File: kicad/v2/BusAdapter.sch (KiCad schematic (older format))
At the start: 53 parts, among them J1 Conn_02x17_Odd_Even, J10 Conn_02x06_Odd_Even, J11 Conn_02x02_Odd_Even, J12 Conn_02x06_Top_Bottom, J2 Conn_02x20_Odd_Even, J3 Conn_02x20_Odd_Even, J4 Conn_02x06_Top_Bottom, J5 Conn_02x06_Top_Bottom, J6 Conn_Coaxial, J7 Conn_Coaxial, J8 Conn_01x02_Male, J9 Conn_01x02_Male, Q1 2N3904, Q2 2N3904, SW1 SW_Push, SW2 SW_Push, U1 74LVC245, U2 74LVC245, U3 74LVC245, U4 IS61C5128AL-10TLI, U5 MCP4822

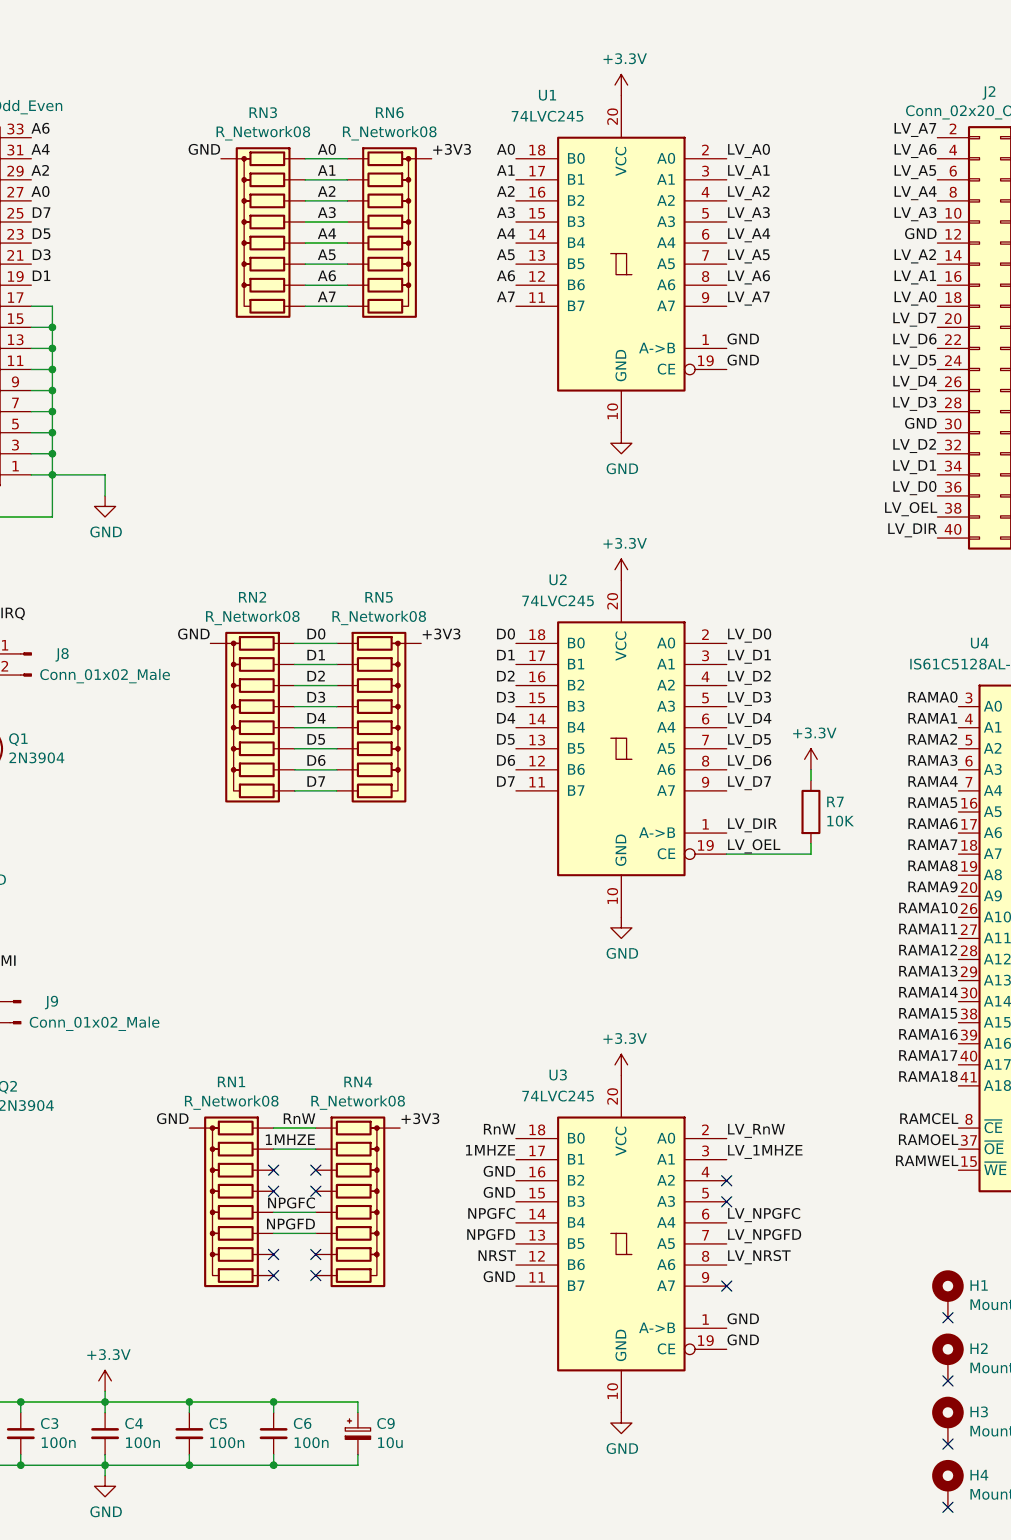
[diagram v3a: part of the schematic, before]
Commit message: PCB v2: Enlarged IDC connector holes; added power connector
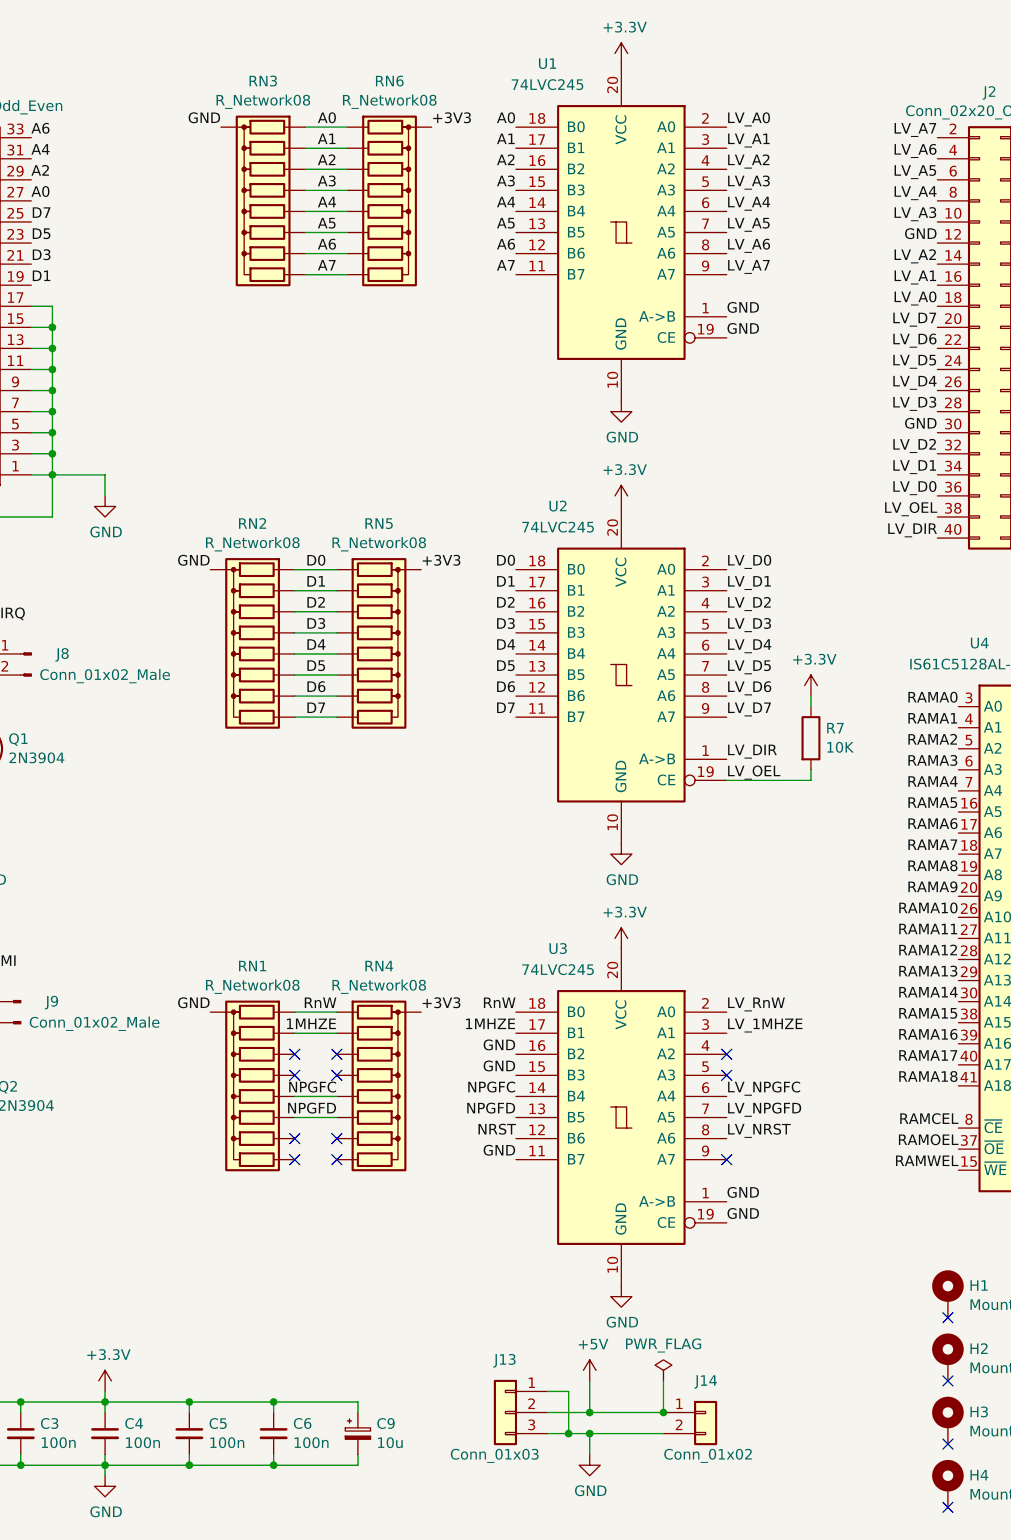
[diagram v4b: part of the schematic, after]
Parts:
- added J13: Conn_01x03, Connector_PinHeader_2.54mm:PinHeader_1x03_P2.54mm_Vertical, symbol Connector_Generic:Conn_01x03
- added J14: Conn_01x02, Connector_PinSocket_2.54mm:PinSocket_1x02_P2.54mm_Vertical, symbol Connector_Generic:Conn_01x02
- J1: footprint Connector_IDC:IDC-Header_2x17_P2.54mm_Horizontal_Lock -> footprints:IDC-Header_2x17_P2.54mm_Horizontal_Lock
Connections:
- net GND: now also J13.1 (Pin_1), J13.3 (Pin_3), J14.2 (Pin_2)
- new net +5V: J13.2 (Pin_2), J14.1 (Pin_1)
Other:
- moved on the sheet: R7, RN1, RN2, RN3, RN4, RN5, RN6, U1, U2, U3

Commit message: PCB v2: Made TSOP-II pads 0.5mm longer on the outside
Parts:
- U4: footprint Package_SO:TSOP-II-44_10.16x18.41mm_P0.8mm -> footprints:TSOP-II-44_10.16x18.41mm_P0.8mm
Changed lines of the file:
@@
 F 0 "U4" H 6200 6350 50  0000 C CNN
 F 1 "IS61C5128AL-10TLI" H 6200 6250 50  0000 C CNN
-F 2 "Package_SO:TSOP-II-44_10.16x18.41mm_P0.8mm" H 6200 6100 50  0001 C CNN
+F 2 "footprints:TSOP-II-44_10.16x18.41mm_P0.8mm" H 6200 6100 50  0001 C CNN
 F 3 "http://www.issi.com/WW/pdf/61-64C5128AL.pdf" H 6700 4950 50  0001 C CNN
 	1    6700 4950

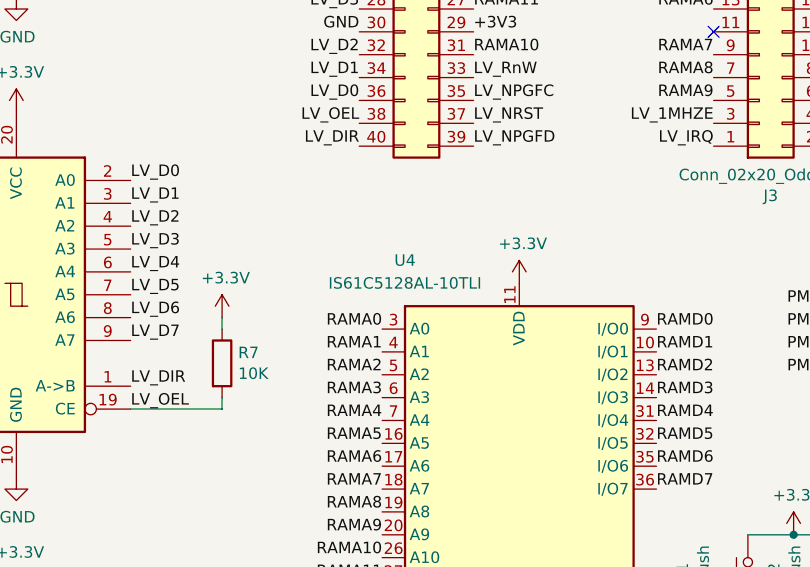
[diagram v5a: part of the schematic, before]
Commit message: Corrected SRAM part number on schematic
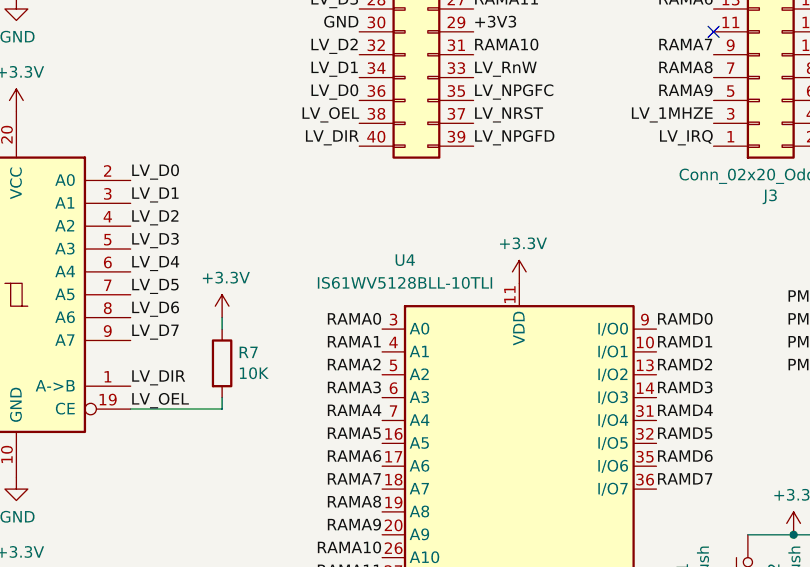
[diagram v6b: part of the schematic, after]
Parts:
- U4: value IS61C5128AL-10TLI -> IS61WV5128BLL-10TLI
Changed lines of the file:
@@
 P 6700 4950
 F 0 "U4" H 6200 6350 50  0000 C CNN
-F 1 "IS61C5128AL-10TLI" H 6200 6250 50  0000 C CNN
+F 1 "IS61WV5128BLL-10TLI" H 6200 6250 50  0000 C CNN
 F 2 "footprints:TSOP-II-44_10.16x18.41mm_P0.8mm" H 6200 6100 50  0001 C CNN
 F 3 "http://www.issi.com/WW/pdf/61-64C5128AL.pdf" H 6700 4950 50  0001 C CNN

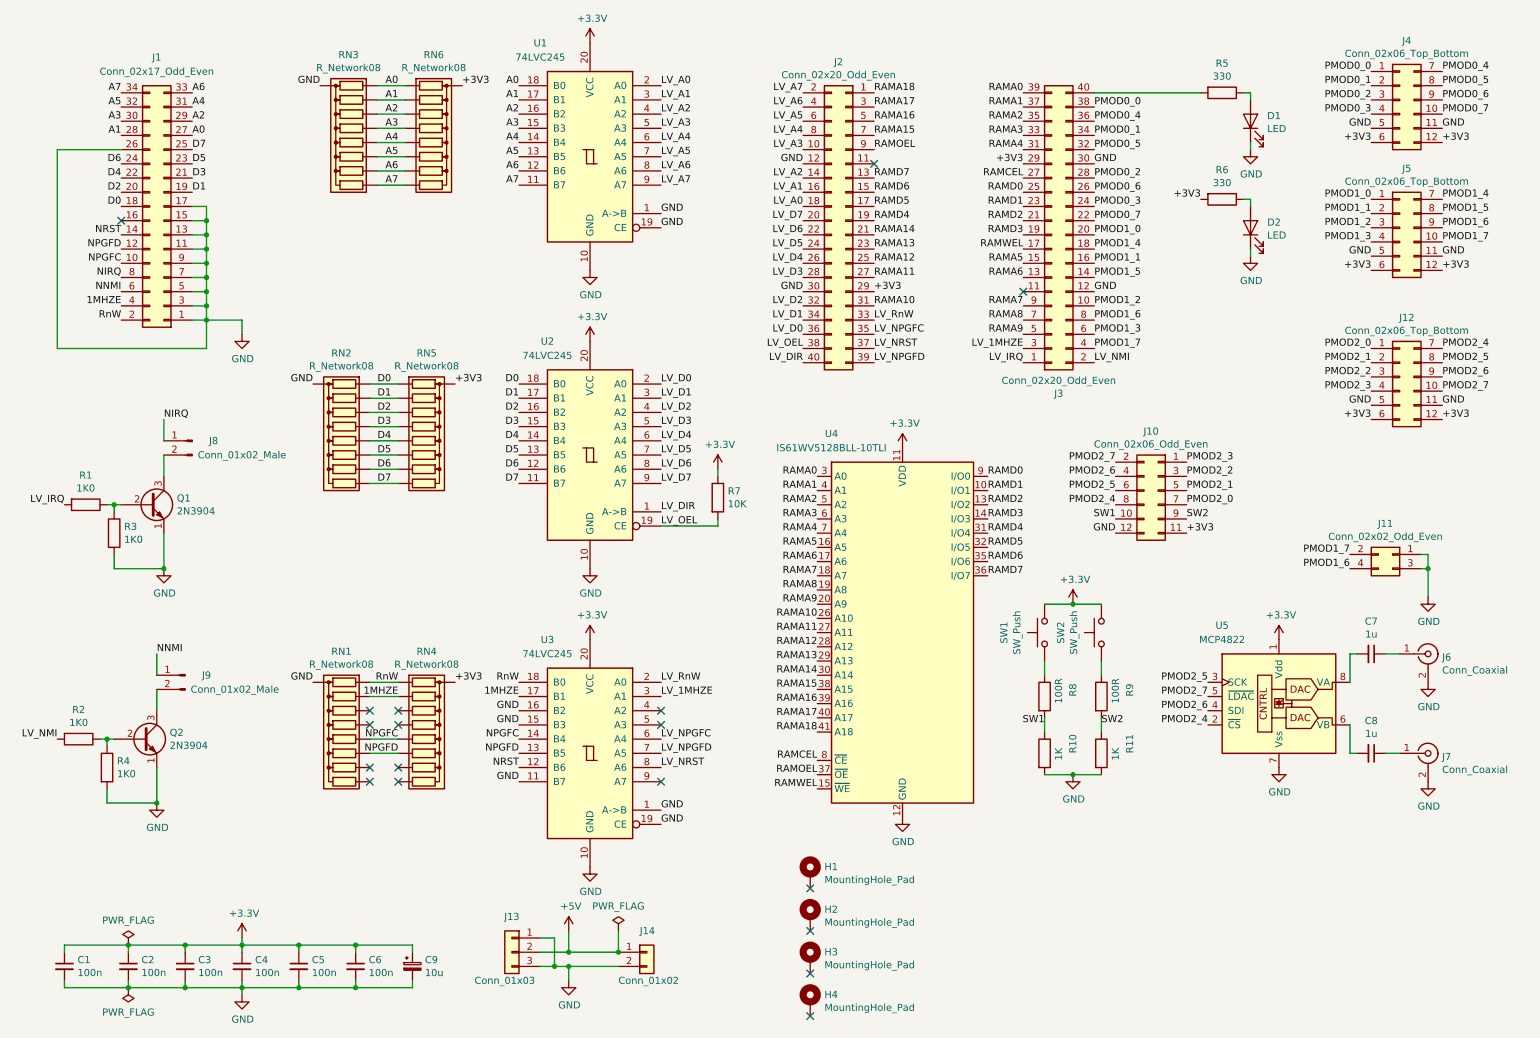
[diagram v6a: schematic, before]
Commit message: Corrected RN and LED values on schematic
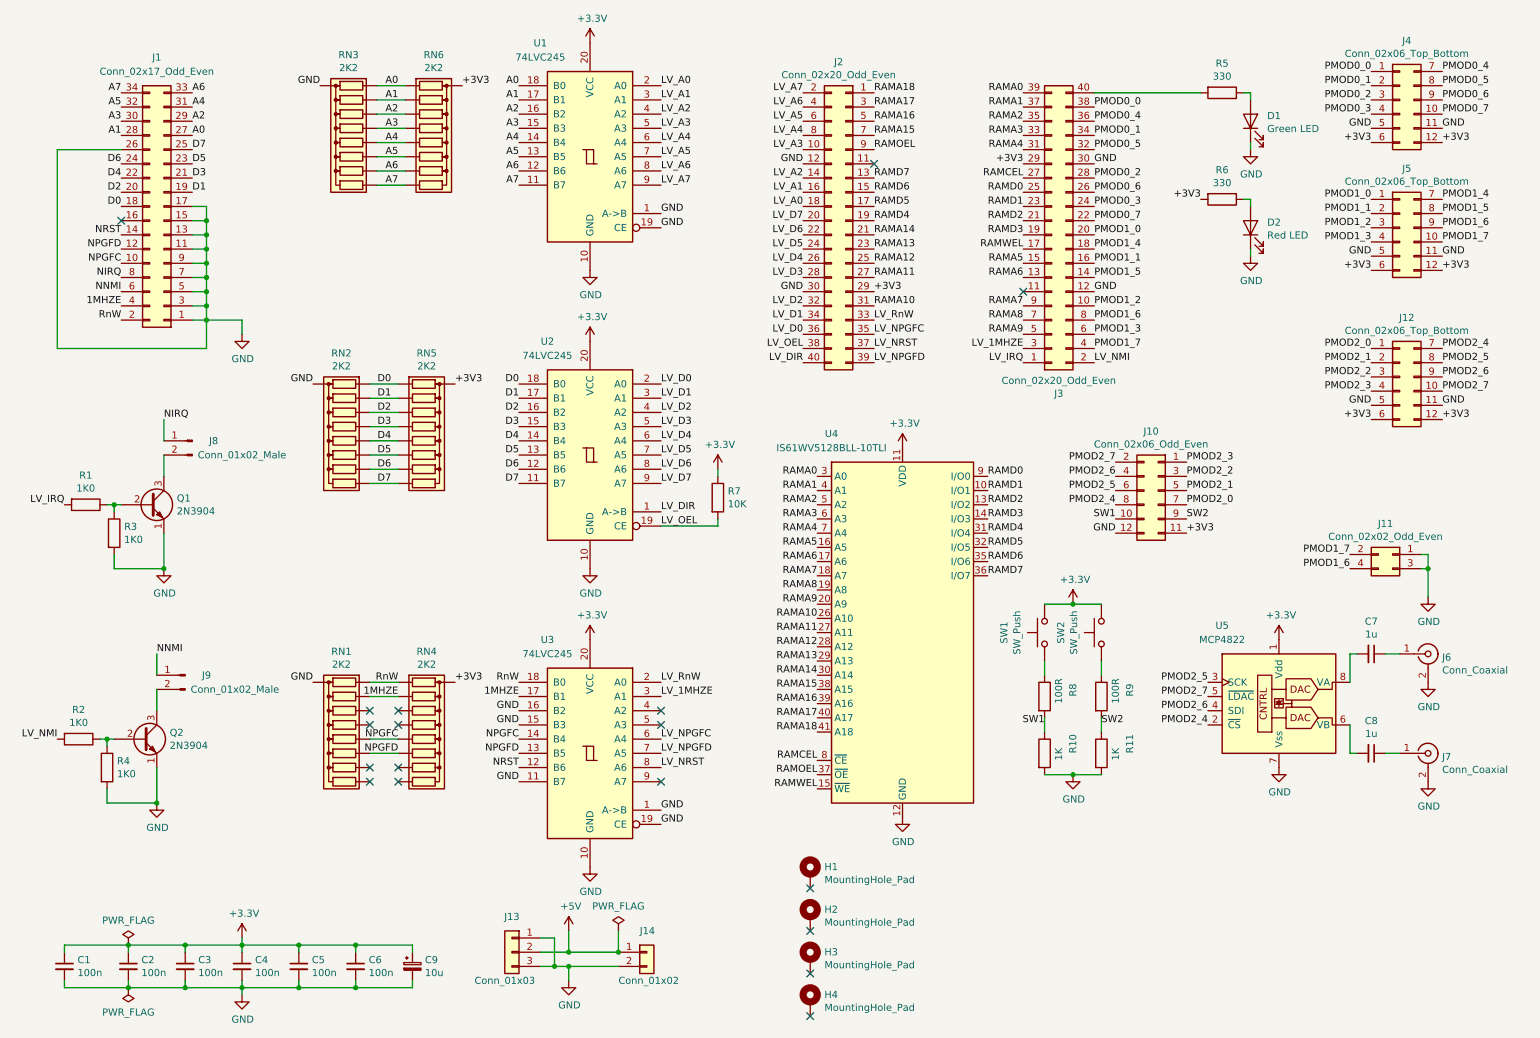
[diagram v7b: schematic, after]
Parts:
- D1: value LED -> Green LED
- D2: value LED -> Red LED
- RN1, RN2, RN3, RN4, RN5, RN6: value R_Network08 -> 2K2
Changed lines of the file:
@@
 P 3400 1500
 F 0 "RN6" V 2783 1500 50  0000 C CNN
-F 1 "R_Network08" V 2874 1500 50  0000 C CNN
+F 1 "2K2" V 2874 1500 50  0000 C CNN
 F 2 "Resistor_THT:R_Array_SIP9" V 3875 1500 50  0001 C CNN
 F 3 "http://www.vishay.com/docs/31509/csc.pdf" H 3400 1500 50  0001 C CNN
@@
 P 2800 1500
 F 0 "RN3" V 2183 1500 50  0000 C CNN
-F 1 "R_Network08" V 2274 1500 50  0000 C CNN
+F 1 "2K2" V 2274 1500 50  0000 C CNN
 F 2 "Resistor_THT:R_Array_SIP9" V 3275 1500 50  0001 C CNN
 F 3 "http://www.vishay.com/docs/31509/csc.pdf" H 2800 1500 50  0001 C CNN
@@
 P 3350 3600
 F 0 "RN5" V 2733 3600 50  0000 C CNN
-F 1 "R_Network08" V 2824 3600 50  0000 C CNN
+F 1 "2K2" V 2824 3600 50  0000 C CNN
 F 2 "Resistor_THT:R_Array_SIP9" V 3825 3600 50  0001 C CNN
 F 3 "http://www.vishay.com/docs/31509/csc.pdf" H 3350 3600 50  0001 C CNN
@@
 P 2750 3600
 F 0 "RN2" V 2133 3600 50  0000 C CNN
-F 1 "R_Network08" V 2224 3600 50  0000 C CNN
+F 1 "2K2" V 2224 3600 50  0000 C CNN
 F 2 "Resistor_THT:R_Array_SIP9" V 3225 3600 50  0001 C CNN
 F 3 "http://www.vishay.com/docs/31509/csc.pdf" H 2750 3600 50  0001 C CNN
@@
 P 3350 5700
 F 0 "RN4" V 2733 5700 50  0000 C CNN
-F 1 "R_Network08" V 2824 5700 50  0000 C CNN
+F 1 "2K2" V 2824 5700 50  0000 C CNN
 F 2 "Resistor_THT:R_Array_SIP9" V 3825 5700 50  0001 C CNN
 F 3 "http://www.vishay.com/docs/31509/csc.pdf" H 3350 5700 50  0001 C CNN
@@
 P 2750 5700
 F 0 "RN1" V 2133 5700 50  0000 C CNN
-F 1 "R_Network08" V 2224 5700 50  0000 C CNN
+F 1 "2K2" V 2224 5700 50  0000 C CNN
 F 2 "Resistor_THT:R_Array_SIP9" V 3225 5700 50  0001 C CNN
 F 3 "http://www.vishay.com/docs/31509/csc.pdf" H 2750 5700 50  0001 C CNN
@@
 P 9150 1350
 F 0 "D1" V 9188 1233 50  0000 R CNN
-F 1 "LED" V 9097 1233 50  0000 R CNN
+F 1 "Green LED" V 9097 1233 50  0000 R CNN
 F 2 "LED_THT:LED_D3.0mm" H 9150 1350 50  0001 C CNN
 F 3 "~" H 9150 1350 50  0001 C CNN
@@
 P 9150 2100
 F 0 "D2" V 9188 1983 50  0000 R CNN
-F 1 "LED" V 9097 1983 50  0000 R CNN
+F 1 "Red LED" V 9097 1983 50  0000 R CNN
 F 2 "LED_THT:LED_D3.0mm" H 9150 2100 50  0001 C CNN
 F 3 "~" H 9150 2100 50  0001 C CNN
